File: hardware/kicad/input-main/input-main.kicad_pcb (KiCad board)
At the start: 2 copper layers, 118 x 118 mm, 74 parts, among them J1 COMMON_MCU_ADAPTER_2x10, Q1 MMBT3904 RGB OE inverter, SW1 MX 1u hot-swap / CPG151101S11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, SW10 MX 1u hot-swap / CPG151101S11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, SW11 MX 2u PTT hot-swap / stabiliz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, SW12 MX 1u hot-swap / CPG151101S11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, SW2 MX 1u hot-swap / CPG151101S11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, SW3 MX 1u hot-swap / CPG151101S11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, SW4 MX 1u hot-swap / CPG151101S11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, SW5 MX 1u hot-swap / CPG151101S11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, SW6 MX 1u hot-swap / CPG151101S11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, SW7 MX 1u hot-swap / CPG151101S11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, SW8 MX 1u hot-swap / CPG151101S11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, SW9 MX 1u hot-swap / CPG151101S11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, U1 MCP23017-E/SO, U2 AT42QT1010-TSHR, U3 TPS2553DBVR, U4 SN74AHCT1G125DBVR

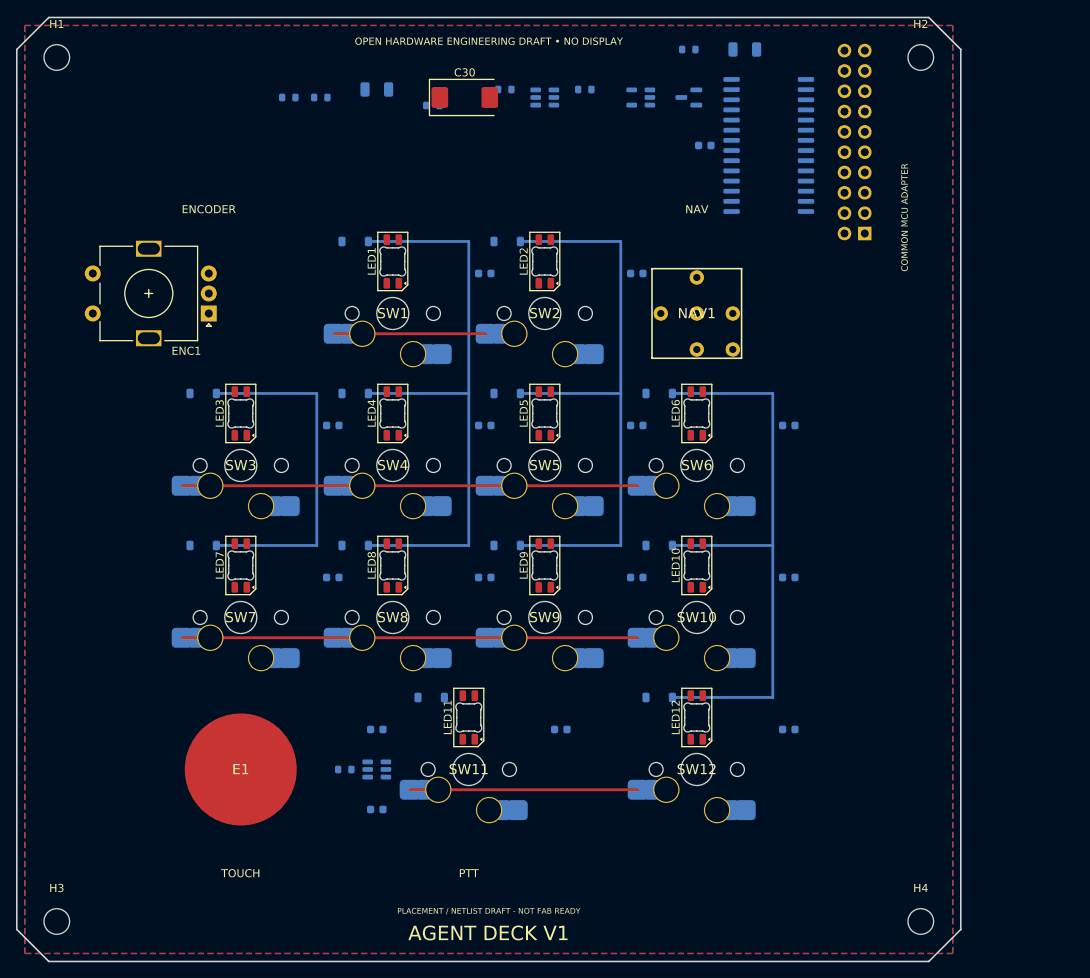
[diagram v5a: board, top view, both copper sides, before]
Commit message: Reduce V1 footprint without shrinking the control grid
Preserve the 19 mm MX lattice while moving the common board and printable fit-check to a 100 mm datum. Repack draft components and make the unmodeled adapter stack an explicit fabrication blocker.

Constraint: Keep 12 hot-swap keys, per-key RGB, encoder, five-way navigation, touch, and the no-display product boundary.

Rejected: 96 mm square | connector, stabilizer, RF, and first-article margins are not frozen.

Confidence: high

Scope-risk: moderate

Directive: Do not fabricate until J1/U1 stack height, USB/RF/battery envelopes, stabilizer geometry, routing, and reviewed LED rules are closed.

Tested: KiCad 10.0.4 ERC 0 on all boards; main DRC 69 documented LED errors and 36 warnings with no short or hole collision; adapters 0 DRC errors; Blender 5.1.2 generated three manifold STLs; 100/100.8/107.8 mm dimensions and six renders verified.

Not-tested: Physical adapter mating, USB cable, antenna, battery, touch overlay, and 2u stabilizer fit.
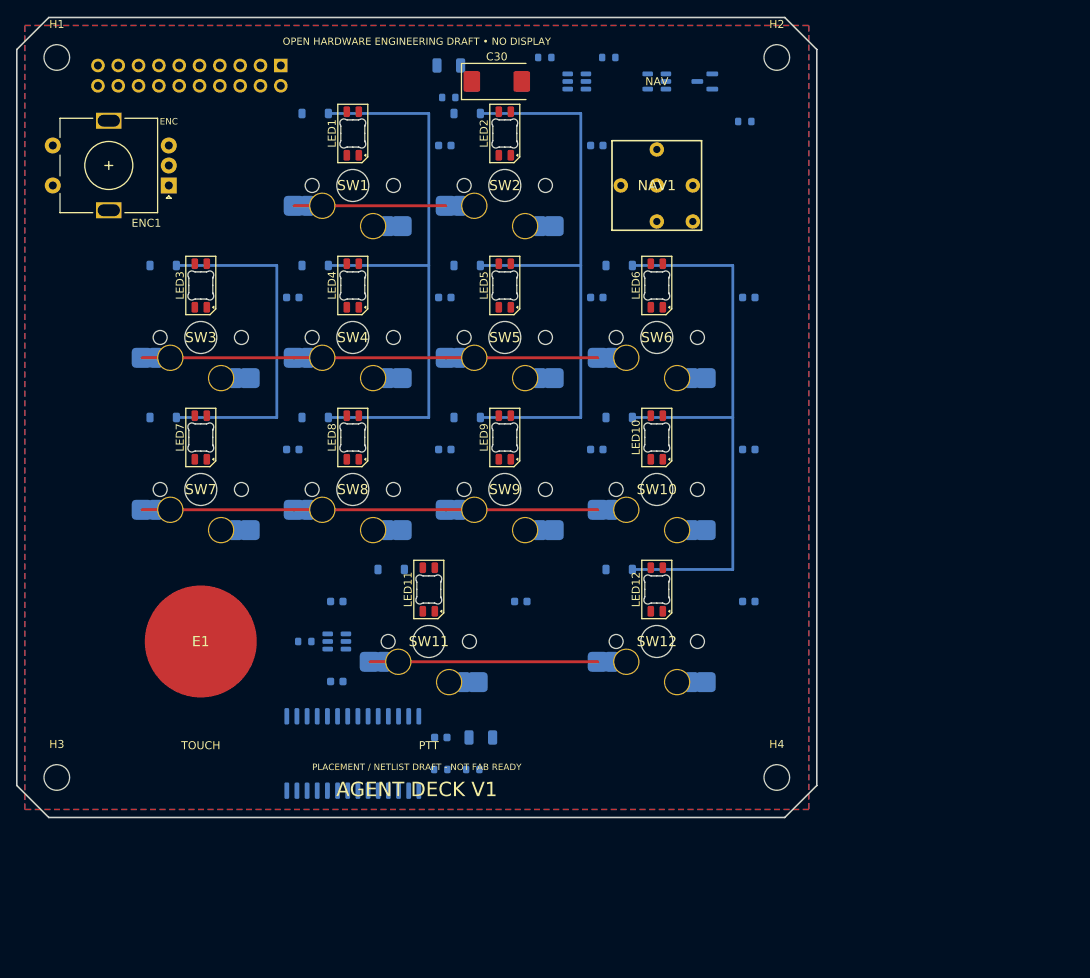
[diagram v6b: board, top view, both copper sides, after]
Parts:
- moved C32 92.1 mm to (68.0, 100.0)
- moved U1 92.1 mm to (52.0, 102.0), turned to 90 degrees
- moved R6 86.1 mm to (63.0, 104.0)
- moved R7 86.1 mm to (67.0, 104.0)
- moved C22 81.0 mm to (63.0, 100.0)
- moved J1 76.0 mm to (43.0, 16.0), turned to 90 degrees
- moved H4 25.5 mm to (105.0, 105.0)
- moved H2 18.0 mm to (105.0, 15.0)
- moved H3 18.0 mm to (15.0, 105.0)
- moved C1 16.8 mm to (63.5, 26.0)
- moved C10 16.8 mm to (101.5, 64.0)
- moved C11 16.8 mm to (73.0, 83.0)
- moved C12 16.8 mm to (101.5, 83.0)
- moved C2 16.8 mm to (82.5, 26.0)
- moved C20 16.8 mm to (50.0, 83.0)
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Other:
- board size 118 x 118 mm -> 100 x 100 mm
- board text added: "ENC"
- board text added: "MCU ADAPTER"
- board text removed: "COMMON MCU ADAPTER"
- board text removed: "ENCODER"

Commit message: Establish a host-verified V1 baseline before physical bring-up
Constraint: The common PCB remains 100 mm square, all controls stay PCB-mounted, and no display is added.
Rejected: Deterministic adapter autorouting | KiCad exposed real escape and via conflicts, so reviewed manual routing remains explicit.
Confidence: medium
Scope-risk: broad
Directive: Do not order boards until all open connections are routed, complete schematics pass parity, exact parts pass sample fit, and physical power/RF/USB/BLE tests succeed.
Tested: KiCad block ERC 0 on three projects; DRC 0 errors with documented warnings and open nets; Blender manifold STL generation; firmware 12/12 normal, sanitized, and embedded-style builds; bridge 41/41 on Python 3.11 and 3.14.
Not-tested: Physical XIAO USB/BLE, RF, battery charging and swelling, touch sensitivity, connector mating, real audio backend, and assembled endurance.
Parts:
- J1: value COMMON_MCU_ADAPTER_2x10 -> COMMON_MCU_ADAPTER_2x10 / Samtec HLE-110-02-G-DV-A fit-check candidate; footprint PinSocket_2x10_P2.54mm_Vertical -> Samtec_HLE-110-02-xxx-DV-A_2x10_P2.54mm_Horizontal
- NAV1: value RKJXM1015004 low-profile stick candidate / land pattern provisional -> RKJXM1015004 catalog-outline fit-check / formal supply spec required; footprint AgentDeck:Nav_RKJXM1015004_ELECTRICAL_PLACEHOLDER -> AgentDeck:Nav_RKJXM1015004_Catalog_Fitcheck
- SW1, SW10, SW12, SW2, SW3, SW4, SW5, SW6, SW7, SW8, SW9: value MX 1u hot-swap / CPG151101S11-16 -> CHERRY MX2A-L1NB / CPG151101S11-16 hot-swap
- SW11: value MX 2u PTT hot-swap / stabilizer TBD / CPG151101S11-16 -> CHERRY MX2A-L1NB 2u PTT hot-swap / KS-52B200T-01 fit-check / CPG151101S11-16
- moved U1 36.0 mm to (88.0, 103.0)
- moved C11 7.62 mm to (80.0, 80.0)
- moved C22 7.00 mm to (70.0, 100.0)
- moved C20 5.00 mm to (45.0, 83.0)
- moved C21 5.00 mm to (45.0, 93.0)
- moved C32 5.00 mm to (63.0, 100.0)
- moved R6 2.00 mm to (65.0, 104.0)
- moved R7 2.00 mm to (69.0, 104.0)
- turned J1 to 180 degrees
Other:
- board text added: "FIT-CHECK / ROUTING DRAFT - NOT FAB READY"
- board text removed: "PLACEMENT / NETLIST DRAFT - NOT FAB READY"
